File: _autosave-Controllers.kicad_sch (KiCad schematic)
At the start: 1 part

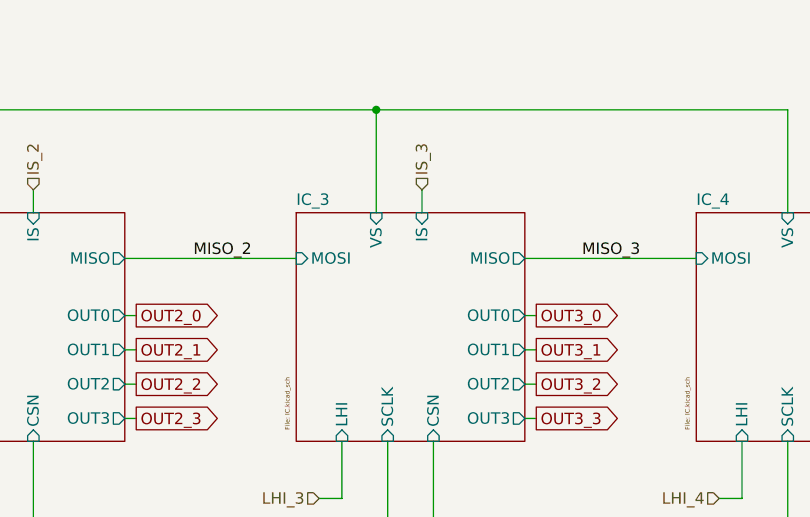
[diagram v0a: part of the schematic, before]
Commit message: Finished schematic
Added UCB C connection
Added CAN
Power ICs schematic fixed
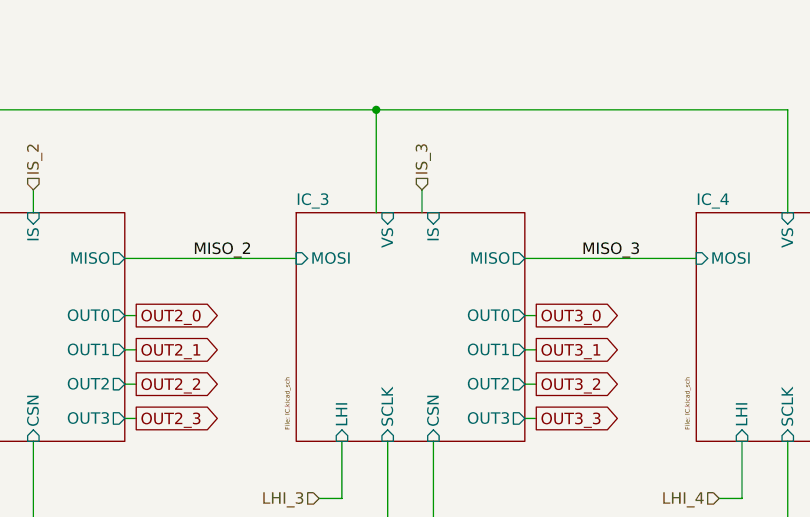
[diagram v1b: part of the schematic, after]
